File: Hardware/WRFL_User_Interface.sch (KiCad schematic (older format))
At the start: 13 parts, among them P16 2x3_2_54_RA_MALE, Q3 SI1012CR, SW1 TSA12110, SW2 EN11-HSB, SW3 TSA12110, U9 S25FL216K0PMFI040

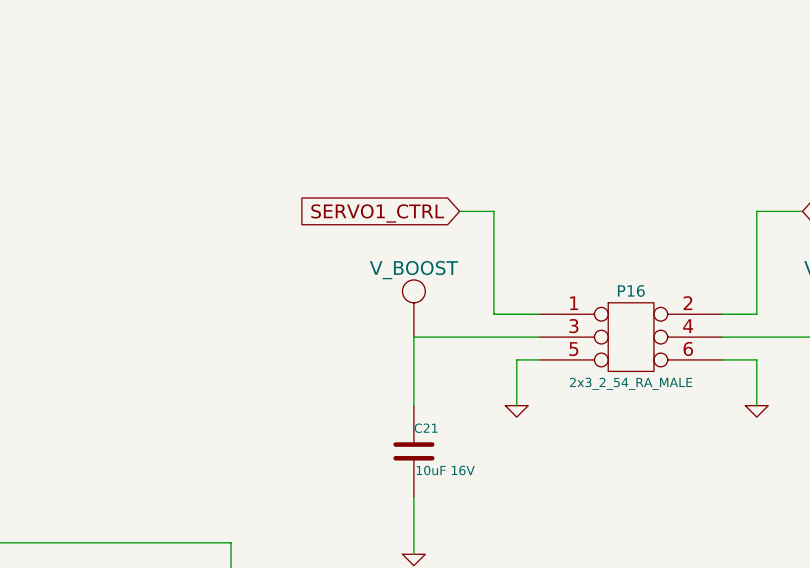
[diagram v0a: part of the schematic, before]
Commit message: 3d Kalman filter progress + minor sch
-moving towards a matrix (CMSIS) based kalman implementation
-cosmetic schematic  changes
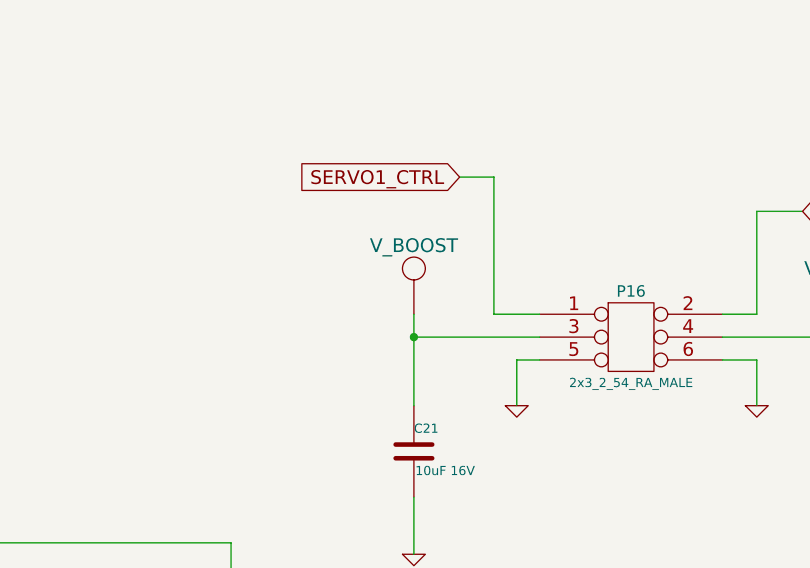
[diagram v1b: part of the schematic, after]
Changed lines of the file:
@@
-EESchema Schematic File Version 2  date 10/31/2013 11:19:55 PM
+EESchema Schematic File Version 2
 LIBS:power
 LIBS:device
@@
 LIBS:WRFL
 LIBS:WRFL-cache
-EELAYER 27 0
+EELAYER 24 0
 EELAYER END
 $Descr A4 11693 8268
@@
 GEN_SSI_CLK
 $Comp
-L VDD_PERIPH #U14
+L VDD_PERIPH #U050
 U 1 1 5251E2C5
 P 950 3350
-F 0 "#U14" H 950 3550 60  0001 C CNN
+F 0 "#U050" H 950 3550 60  0001 C CNN
 F 1 "VDD_PERIPH" H 950 3450 60  0000 C CNN
 F 2 "~" H 950 3350 60  0000 C CNN
@@
 $EndComp
 $Comp
-L VDD_PERIPH #U18
+L VDD_PERIPH #U051
 U 1 1 5251E301
 P 9300 1550
-F 0 "#U18" H 9300 1750 60  0001 C CNN
+F 0 "#U051" H 9300 1750 60  0001 C CNN
 F 1 "VDD_PERIPH" H 9300 1650 60  0000 C CNN
 F 2 "~" H 9300 1550 60  0000 C CNN
@@
 $EndComp
 $Comp
-L GND #PWR33
+L GND #PWR052
 U 1 1 5251E310
 P 950 4350
-F 0 "#PWR33" H 950 4350 30  0001 C CNN
+F 0 "#PWR052" H 950 4350 30  0001 C CNN
 F 1 "GND" H 950 4280 30  0001 C CNN
 F 2 "" H 950 4350 60  0000 C CNN
@@
 $EndComp
 $Comp
-L GND #PWR34
+L GND #PWR053
 U 1 1 5251E31F
 P 2600 6250
-F 0 "#PWR34" H 2600 6250 30  0001 C CNN
+F 0 "#PWR053" H 2600 6250 30  0001 C CNN
 F 1 "GND" H 2600 6180 30  0001 C CNN
 F 2 "" H 2600 6250 60  0000 C CNN
@@
 $EndComp
 $Comp
-L GND #PWR37
+L GND #PWR054
 U 1 1 5251E32E
 P 4450 5950
-F 0 "#PWR37" H 4450 5950 30  0001 C CNN
+F 0 "#PWR054" H 4450 5950 30  0001 C CNN
 F 1 "GND" H 4450 5880 30  0001 C CNN
 F 2 "" H 4450 5950 60  0000 C CNN
@@
 $EndComp
 $Comp
-L GND #PWR38
+L GND #PWR055
 U 1 1 5251E33D
 P 6500 6400
-F 0 "#PWR38" H 6500 6400 30  0001 C CNN
+F 0 "#PWR055" H 6500 6400 30  0001 C CNN
 F 1 "GND" H 6500 6330 30  0001 C CNN
 F 2 "" H 6500 6400 60  0000 C CNN
@@
 $EndComp
 $Comp
-L GND #PWR36
+L GND #PWR056
 U 1 1 5251E34C
 P 3150 2500
-F 0 "#PWR36" H 3150 2500 30  0001 C CNN
+F 0 "#PWR056" H 3150 2500 30  0001 C CNN
 F 1 "GND" H 3150 2430 30  0001 C CNN
 F 2 "" H 3150 2500 60  0000 C CNN
@@
 $EndComp
 $Comp
-L GND #PWR39
+L GND #PWR057
 U 1 1 5251E35B
 P 7500 2700
-F 0 "#PWR39" H 7500 2700 30  0001 C CNN
+F 0 "#PWR057" H 7500 2700 30  0001 C CNN
 F 1 "GND" H 7500 2630 30  0001 C CNN
 F 2 "" H 7500 2700 60  0000 C CNN
@@
 $EndComp
 $Comp
-L GND #PWR35
+L GND #PWR058
 U 1 1 5251E3CC
 P 2950 4350
-F 0 "#PWR35" H 2950 4350 30  0001 C CNN
+F 0 "#PWR058" H 2950 4350 30  0001 C CNN
 F 1 "GND" H 2950 4280 30  0001 C CNN
 F 2 "" H 2950 4350 60  0000 C CNN
@@
 $EndComp
 $Comp
-L GND #PWR43
+L GND #PWR059
 U 1 1 5251EA53
 P 10150 2500
-F 0 "#PWR43" H 10150 2500 30  0001 C CNN
+F 0 "#PWR059" H 10150 2500 30  0001 C CNN
 F 1 "GND" H 10150 2430 30  0001 C CNN
 F 2 "" H 10150 2500 60  0000 C CNN
@@
 	10150 1850 10150 1900
 $Comp
-L VDD_PERIPH #U16
+L VDD_PERIPH #U060
 U 1 1 5251EAB9
 P 5950 1150
-F 0 "#U16" H 5950 1350 60  0001 C CNN
+F 0 "#U060" H 5950 1350 60  0001 C CNN
 F 1 "VDD_PERIPH" H 5950 1250 60  0000 C CNN
 F 2 "~" H 5950 1150 60  0000 C CNN
@@
 $EndComp
 $Comp
-L GND #PWR42
+L GND #PWR061
 U 1 1 52523A67
 P 9800 4700
-F 0 "#PWR42" H 9800 4700 30  0001 C CNN
+F 0 "#PWR061" H 9800 4700 30  0001 C CNN
 F 1 "GND" H 9800 4630 30  0001 C CNN
 F 2 "" H 9800 4700 60  0000 C CNN
@@
 $EndComp
 $Comp
-L GND #PWR41
+L GND #PWR062
 U 1 1 52523A76
 P 8750 4700
-F 0 "#PWR41" H 8750 4700 30  0001 C CNN
+F 0 "#PWR062" H 8750 4700 30  0001 C CNN
 F 1 "GND" H 8750 4630 30  0001 C CNN
 F 2 "" H 8750 4700 60  0000 C CNN
@@
 	9800 4500 9800 4700
 $Comp
-L V_BOOST #U17
+L V_BOOST #U063
 U 1 1 52523B29
-P 8300 4200
-F 0 "#U17" H 8300 4400 60  0001 C CNN
-F 1 "V_BOOST" H 8300 4300 60  0000 C CNN
-F 2 "~" H 8300 4200 60  0000 C CNN
-F 3 "~" H 8300 4200 60  0000 C CNN
-	1    8300 4200
-	1    0    0    -1
-$EndComp
-$Comp
-L V_BOOST #U19
+P 8300 4100
+F 0 "#U063" H 8300 4300 60  0001 C CNN
+F 1 "V_BOOST" H 8300 4200 60  0000 C CNN
+F 2 "~" H 8300 4100 60  0000 C CNN
+F 3 "~" H 8300 4100 60  0000 C CNN
+	1    8300 4100
+	1    0    0    -1
+$EndComp
+$Comp
+L V_BOOST #U064
 U 1 1 52523B38
 P 10200 4200
-F 0 "#U19" H 10200 4400 60  0001 C CNN
+F 0 "#U064" H 10200 4400 60  0001 C CNN
 F 1 "V_BOOST" H 10200 4300 60  0000 C CNN
 F 2 "~" H 10200 4200 60  0000 C CNN
@@
 Wire Wire Line
 	9650 4400 10200 4400
-Wire Wire Line
-	8300 4400 8850 4400
-Text GLabel 8500 3850 0    60   Input ~ 0
+Text GLabel 8500 3700 0    60   Input ~ 0
 SERVO1_CTRL
 Text GLabel 10000 3850 2    60   Input ~ 0
@@
 	9800 4300 9650 4300
 Wire Wire Line
-	8500 3850 8650 3850
-Wire Wire Line
-	8650 3850 8650 4300
+	8650 3700 8650 4300
 Wire Wire Line
 	8650 4300 8850 4300
@@
 $EndComp
 $Comp
-L GND #PWR40
+L GND #PWR065
 U 1 1 52526592
 P 8300 5350
-F 0 "#PWR40" H 8300 5350 30  0001 C CNN
+F 0 "#PWR065" H 8300 5350 30  0001 C CNN
 F 1 "GND" H 8300 5280 30  0001 C CNN
 F 2 "" H 8300 5350 60  0000 C CNN
@@
 $EndComp
 Wire Wire Line
-	8300 4700 8300 4400
+	8300 4700 8300 4300
 Wire Wire Line
 	8300 5100 8300 5350
@@
 Connection ~ 9300 1850
 $Comp
-L VDD_PERIPH #U15
+L VDD_PERIPH #U066
 U 1 1 525D7AAA
 P 3150 6600
-F 0 "#U15" H 3150 6800 60  0001 C CNN
+F 0 "#U066" H 3150 6800 60  0001 C CNN
 F 1 "VDD_PERIPH" H 3150 6700 60  0000 C CNN
 F 2 "~" H 3150 6600 60  0000 C CNN
@@
 Wire Wire Line
 	6200 5700 6550 5700
+Wire Wire Line
+	8650 3700 8500 3700
+Wire Wire Line
+	8850 4400 8300 4400
+Connection ~ 8300 4400
 $EndSCHEMATC
